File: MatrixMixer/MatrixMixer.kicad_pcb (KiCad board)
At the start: 2 copper layers, 60.5 x 128.5 mm, 22 parts

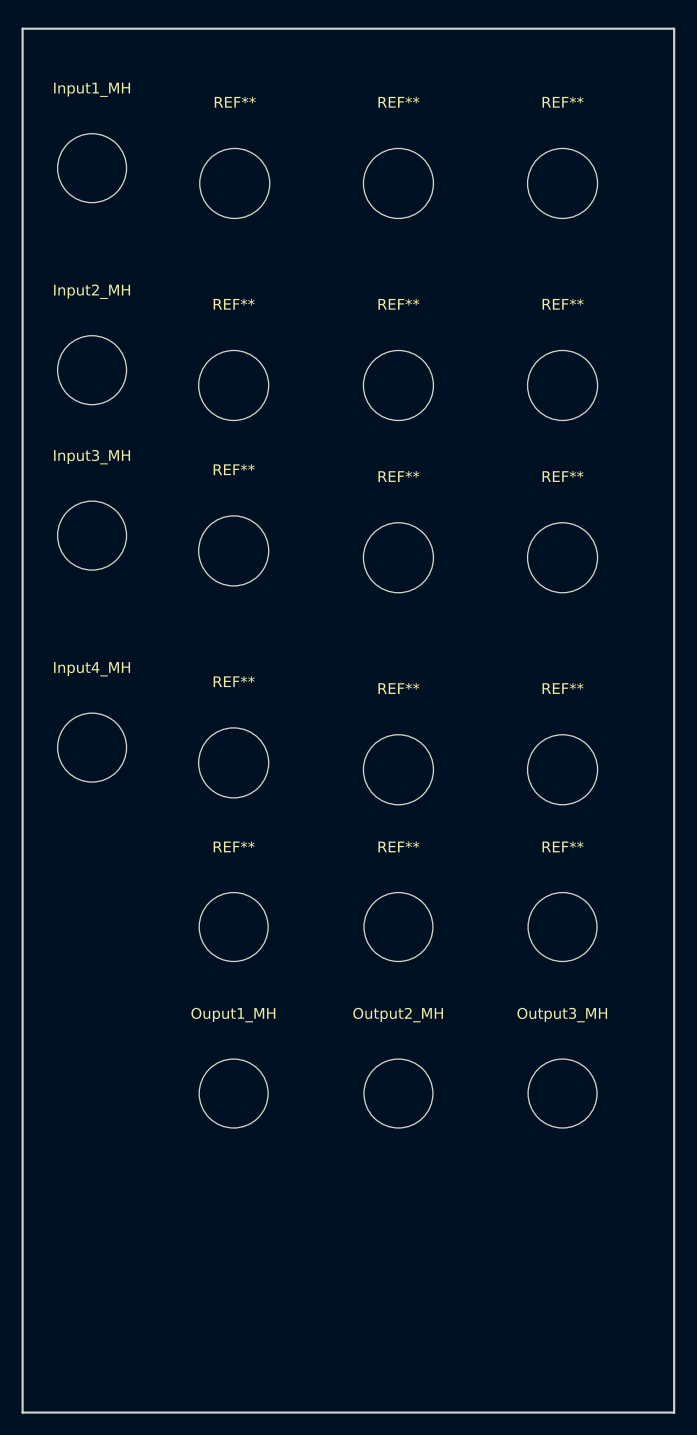
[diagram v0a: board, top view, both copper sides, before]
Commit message: faceplate aligned with potiemeters, jacks and switches
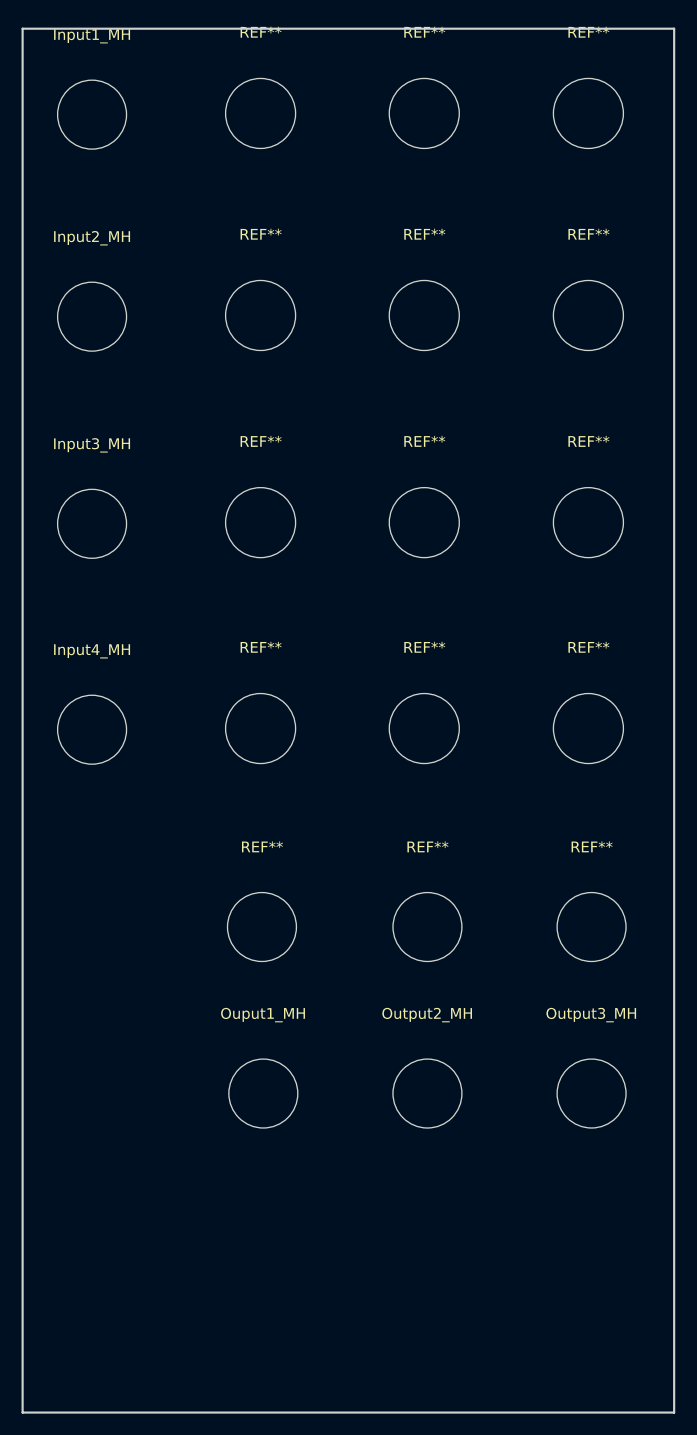
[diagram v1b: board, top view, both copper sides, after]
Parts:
- moved REF** 6.96 mm to (123.6, 59.1)
- moved REF** 6.93 mm to (123.6, 40.4)
- moved REF** 6.93 mm to (154.0, 40.4)
- moved REF** 6.93 mm to (138.8, 40.4)
- moved REF** 6.93 mm to (138.8, 59.1)
- moved REF** 6.93 mm to (154.0, 59.1)
- moved Input1_MH 4.97 mm to (108.0, 40.5)
- moved Input2_MH 4.97 mm to (108.0, 59.2)
- moved REF** 4.52 mm to (138.8, 97.5)
- moved REF** 4.52 mm to (154.0, 97.5)
- moved REF** 4.05 mm to (123.6, 97.5)
- moved REF** 4.05 mm to (154.0, 78.4)
- moved REF** 4.05 mm to (138.8, 78.4)
- moved REF** 3.63 mm to (123.6, 78.4)
- moved Ouput1_MH 2.75 mm to (123.9, 131.4)
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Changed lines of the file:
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@@
 	(footprint "MountingHole:MountingHole_6.5mm"
 		(layer "F.Cu")
-		(at 121.098 80.99)
+		(at 123.598 78.3645)
 		(descr "Mounting Hole 6.5mm, no annular")
 		(tags "mounting hole 6.5mm no annular")
@@
 	(footprint "MountingHole:MountingHole_6.4mm_M6"
 		(layer "F.Cu")
-		(at 121.098 115.915)
+		(at 123.725 115.915)
 		(descr "Mounting Hole 6.4mm, no annular, M6")
 		(tags "mounting hole 6.4mm no annular m6")
@@
 	(footprint "MountingHole:MountingHole_6.4mm_M6"
 		(layer "F.Cu")
-		(at 151.638 131.376)
+		(at 154.332 131.376)
 		(descr "Mounting Hole 6.4mm, no annular, M6")
 		(tags "mounting hole 6.4mm no annular m6")
@@
 	(footprint "MountingHole:MountingHole_6.5mm"
 		(layer "F.Cu")
-		(at 151.638 81.625)
+		(at 154.038 78.3645)
 		(descr "Mounting Hole 6.5mm, no annular")
 		(tags "mounting hole 6.5mm no annular")
@@
 	(footprint "MountingHole:MountingHole_6.5mm"
 		(layer "F.Cu")
-		(at 121.198 46.87)
+		(at 123.598 40.37)
 		(descr "Mounting Hole 6.5mm, no annular")
 		(tags "mounting hole 6.5mm no annular")
@@
 	(footprint "MountingHole:MountingHole_6.5mm"
 		(layer "F.Cu")
-		(at 151.638 46.87)
+		(at 154.038 40.37)
 		(descr "Mounting Hole 6.5mm, no annular")
 		(tags "mounting hole 6.5mm no annular")
@@
 	(footprint "MountingHole:MountingHole_6.5mm"
 		(layer "F.Cu")
-		(at 136.398 46.87)
+		(at 138.798 40.37)
 		(descr "Mounting Hole 6.5mm, no annular")
 		(tags "mounting hole 6.5mm no annular")
@@
 	(footprint "MountingHole:MountingHole_6.5mm"
 		(layer "F.Cu")
-		(at 136.398 81.625)
+		(at 138.798 78.3645)
 		(descr "Mounting Hole 6.5mm, no annular")
 		(tags "mounting hole 6.5mm no annular")
@@
 	(footprint "MountingHole:MountingHole_6.5mm"
 		(layer "F.Cu")
-		(at 151.638 65.63)
+		(at 154.038 59.13)
 		(descr "Mounting Hole 6.5mm, no annular")
 		(tags "mounting hole 6.5mm no annular")
@@
 	(footprint "MountingHole:MountingHole_6.4mm_M6"
 		(layer "F.Cu")
-		(at 107.95 64.21)
+		(at 107.95 59.24)
 		(descr "Mounting Hole 6.4mm, no annular, M6")
 		(tags "mounting hole 6.4mm no annular m6")
@@
 	(footprint "MountingHole:MountingHole_6.4mm_M6"
 		(layer "F.Cu")
-		(at 107.95 45.45)
+		(at 107.95 40.48)
 		(descr "Mounting Hole 6.4mm, no annular, M6")
 		(tags "mounting hole 6.4mm no annular m6")
@@
 			(layers "*.Cu" "*.Mask")
 		)
+		(model "${KIPRJMOD}/3dmodels/FrontBoard.step"
+			(offset
+				(xyz -108 39.5 -13.5)
+			)
+			(scale
+				(xyz 1 1 1)
+			)
+			(rotate
+				(xyz 0 0 0)
+			)
+		)
 	)
 	(footprint "MountingHole:MountingHole_6.5mm"
 		(layer "F.Cu")
-		(at 121.098 100.675)
+		(at 123.598 97.484)
 		(descr "Mounting Hole 6.5mm, no annular")
 		(tags "mounting hole 6.5mm no annular")
@@
 	(footprint "MountingHole:MountingHole_6.4mm_M6"
 		(layer "F.Cu")
-		(at 136.398 115.915)
+		(at 139.092 115.915)
 		(descr "Mounting Hole 6.4mm, no annular, M6")
 		(tags "mounting hole 6.4mm no annular m6")
@@
 	(footprint "MountingHole:MountingHole_6.5mm"
 		(layer "F.Cu")
-		(at 136.398 65.63)
+		(at 138.798 59.13)
 		(descr "Mounting Hole 6.5mm, no annular")
 		(tags "mounting hole 6.5mm no annular")
@@
 	(footprint "MountingHole:MountingHole_6.5mm"
 		(layer "F.Cu")
-		(at 136.398 101.31)
+		(at 138.798 97.484)
 		(descr "Mounting Hole 6.5mm, no annular")
 		(tags "mounting hole 6.5mm no annular")
@@
 	(footprint "MountingHole:MountingHole_6.4mm_M6"
 		(layer "F.Cu")
-		(at 136.398 131.376)
+		(at 139.092 131.376)
 		(descr "Mounting Hole 6.4mm, no annular, M6")
 		(tags "mounting hole 6.4mm no annular m6")
@@
 	(footprint "MountingHole:MountingHole_6.5mm"
 		(layer "F.Cu")
-		(at 121.098 65.63)
+		(at 123.598 59.13)
 		(descr "Mounting Hole 6.5mm, no annular")
 		(tags "mounting hole 6.5mm no annular")
@@
 	(footprint "MountingHole:MountingHole_6.4mm_M6"
 		(layer "F.Cu")
-		(at 151.638 115.915)
+		(at 154.332 115.915)
 		(descr "Mounting Hole 6.4mm, no annular, M6")
 		(tags "mounting hole 6.4mm no annular m6")
@@
 	(footprint "MountingHole:MountingHole_6.5mm"
 		(layer "F.Cu")
-		(at 151.638 101.31)
+		(at 154.038 97.484)
 		(descr "Mounting Hole 6.5mm, no annular")
 		(tags "mounting hole 6.5mm no annular")
@@
 	(footprint "MountingHole:MountingHole_6.4mm_M6"
 		(layer "F.Cu")
-		(at 107.95 99.255)
+		(at 107.95 97.594)
 		(descr "Mounting Hole 6.4mm, no annular, M6")
 		(tags "mounting hole 6.4mm no annular m6")
@@
 	(footprint "MountingHole:MountingHole_6.4mm_M6"
 		(layer "F.Cu")
-		(at 107.95 79.57)
+		(at 107.95 78.4745)
 		(descr "Mounting Hole 6.4mm, no annular, M6")
 		(tags "mounting hole 6.4mm no annular m6")
@@
 	(footprint "MountingHole:MountingHole_6.4mm_M6"
 		(layer "F.Cu")
-		(at 121.098 131.376)
+		(at 123.852 131.376)
 		(descr "Mounting Hole 6.4mm, no annular, M6")
 		(tags "mounting hole 6.4mm no annular m6")

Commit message: replaced SPST swtiches with sub-toggle, alinged switch faceplace holes, updated 3d models
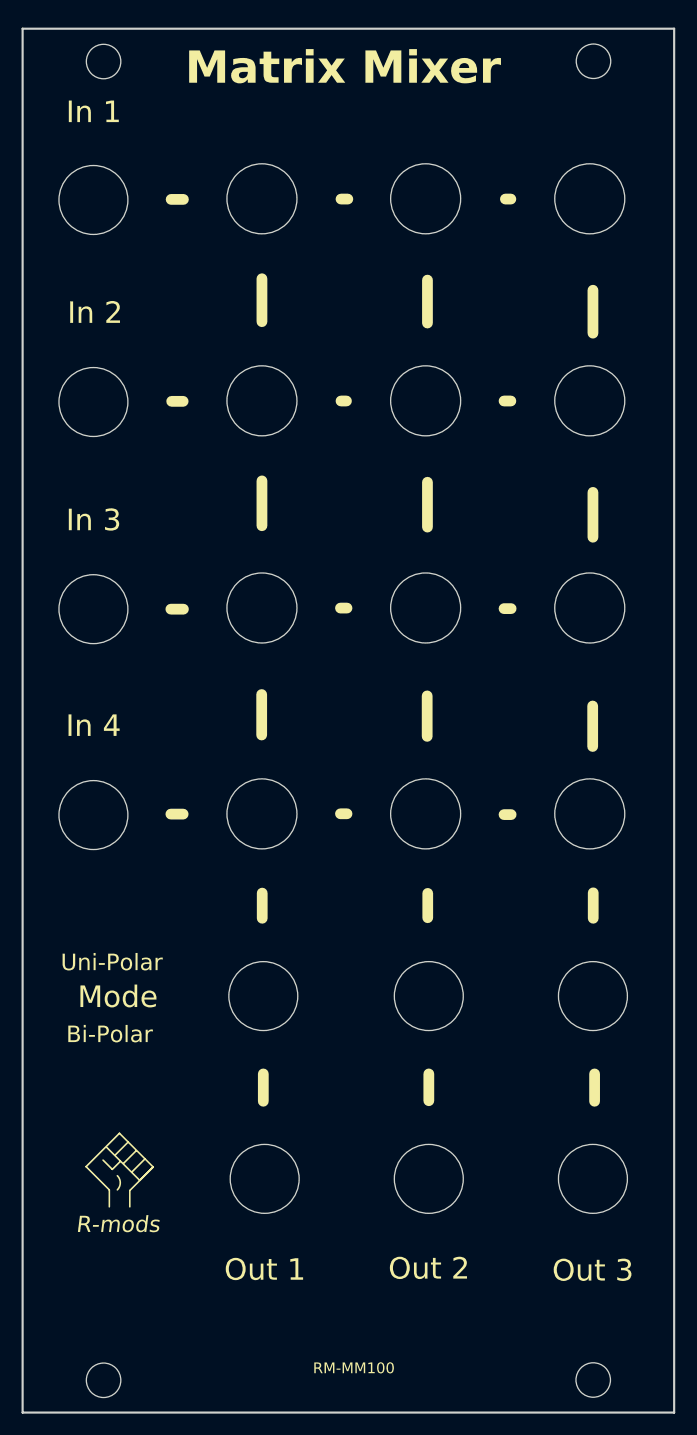
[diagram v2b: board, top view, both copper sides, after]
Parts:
- added fpmht: MountingHole_3.2mm_M3, MountingHole:MountingHole_3.2mm_M3, F.Cu at (109.0, 35.5)
- added fpmht: MountingHole_3.2mm_M3, MountingHole:MountingHole_3.2mm_M3, F.Cu at (154.5, 35.5)
- added fpmht3: MountingHole_3.2mm_M3, MountingHole:MountingHole_3.2mm_M3, F.Cu at (109.0, 158.0)
- added fpmht4: MountingHole_3.2mm_M3, MountingHole:MountingHole_3.2mm_M3, F.Cu at (154.5, 158.0)
- In 1: renamed from Input1_MH
- In 2: renamed from Input2_MH
- In 3: renamed from Input3_MH
- In 4: renamed from Input4_MH
- Out 1: renamed from Ouput1_MH
- Out 2: renamed from Output2_MH
- Out 3: renamed from Output3_MH
- moved Out 3 7.93 mm to (154.5, 139.3)
- moved REF** 7.93 mm to (123.7, 48.3)
- moved REF** 7.93 mm to (123.7, 105.4)
- moved In 1 7.93 mm to (108.1, 48.4)
- moved In 4 7.93 mm to (108.1, 105.5)
- moved Out 1 7.93 mm to (124.0, 139.3)
- moved Out 2 7.93 mm to (139.2, 139.3)
- moved REF** 7.93 mm to (138.9, 105.4)
- moved REF** 7.93 mm to (154.2, 105.4)
- moved REF** 7.93 mm to (154.2, 48.3)
- moved REF** 7.93 mm to (138.9, 48.3)
- moved REF** 7.93 mm to (123.7, 67.1)
- moved In 2 7.93 mm to (108.1, 67.2)
- moved REF** 7.93 mm to (154.2, 67.1)
- moved REF** 7.93 mm to (138.9, 67.1)
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- renumbered REF** to Mode
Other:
- board text added: "Bi-Polar"
- board text added: "Matrix Mixer"
- board text added: "R-mods"
- board text added: "RM-MM100"
- board text added: "RM-MMB3-2024-v1.0.0"
- board text added: "Uni-Polar"
